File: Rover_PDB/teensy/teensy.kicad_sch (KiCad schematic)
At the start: 14 parts, among them J1 Conn_01x04, J2 Conn_01x04, J3 Conn_01x04, M1 Fan, M2 Fan, M3 Fan, Q1 Q_NMOS, Q2 Q_NMOS, U1 Teensy4.1, U2 MCP9808_MSOP

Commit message: update
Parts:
- removed Q1, Q2: Q_NMOS, Package_TO_SOT_THT:TO-92_Inline, symbol Device:Q_NMOS
- added C2, C4: 100nF, Capacitor_SMD:C_01005_0402Metric, symbol Device:C_Small
- added C3: 50nF, Capacitor_SMD:C_01005_0402Metric, symbol Device:C_Small
- added Q1, Q2: NMOS, Package_TO_SOT_THT:TO-220-3_Vertical, symbol Simulation_SPICE:NMOS
- C1: footprint Package_TO_SOT_SMD:SOT-23-6 -> Capacitor_SMD:C_01005_0402Metric
- R1, R2, R3: footprint Package_DIP:DIP-8_W7.62mm -> Resistor_SMD:R_01005_0402Metric
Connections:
- net GND: now also C1.1, C1.2, J3.2 (Pin_2), U1.45 (23_A9_CRX1_MCLK1), U1.47 (GND), U1.58 (GND), U2.8 (V_{DD}), C2.2, C3.2, Q1.3 (S), Q2.3 (S)
- net SCL_BMS_TEAM: no longer U1.41 (19_A5_SCL), U2.2 (SCL)
- net SDA_BMS_TEAM: no longer U1.40 (18_A4_SDA), U2.1 (SDA)
- net at M1.2 (-), M2.2 (-), M3.2 (-): now also Q2.1 (D)
- net at R2.2: now also C3.1, Q1.1 (D), Q2.2 (G)
- net at R1.1, U1.44 (22_A8_CTX1): now also C2.1
- net at U1.48 (VIN): now also C4.1, C4.2
- net +3V3: now reaches U1.51 (3V3)
- net +3V3: now also J3.1 (Pin_1)
- net at R1.2: now also Q1.2 (G)
- new net SCL: U2.2 (SCL)
- new net SDA: U2.1 (SDA)
- no-connect marks 62 -> 57

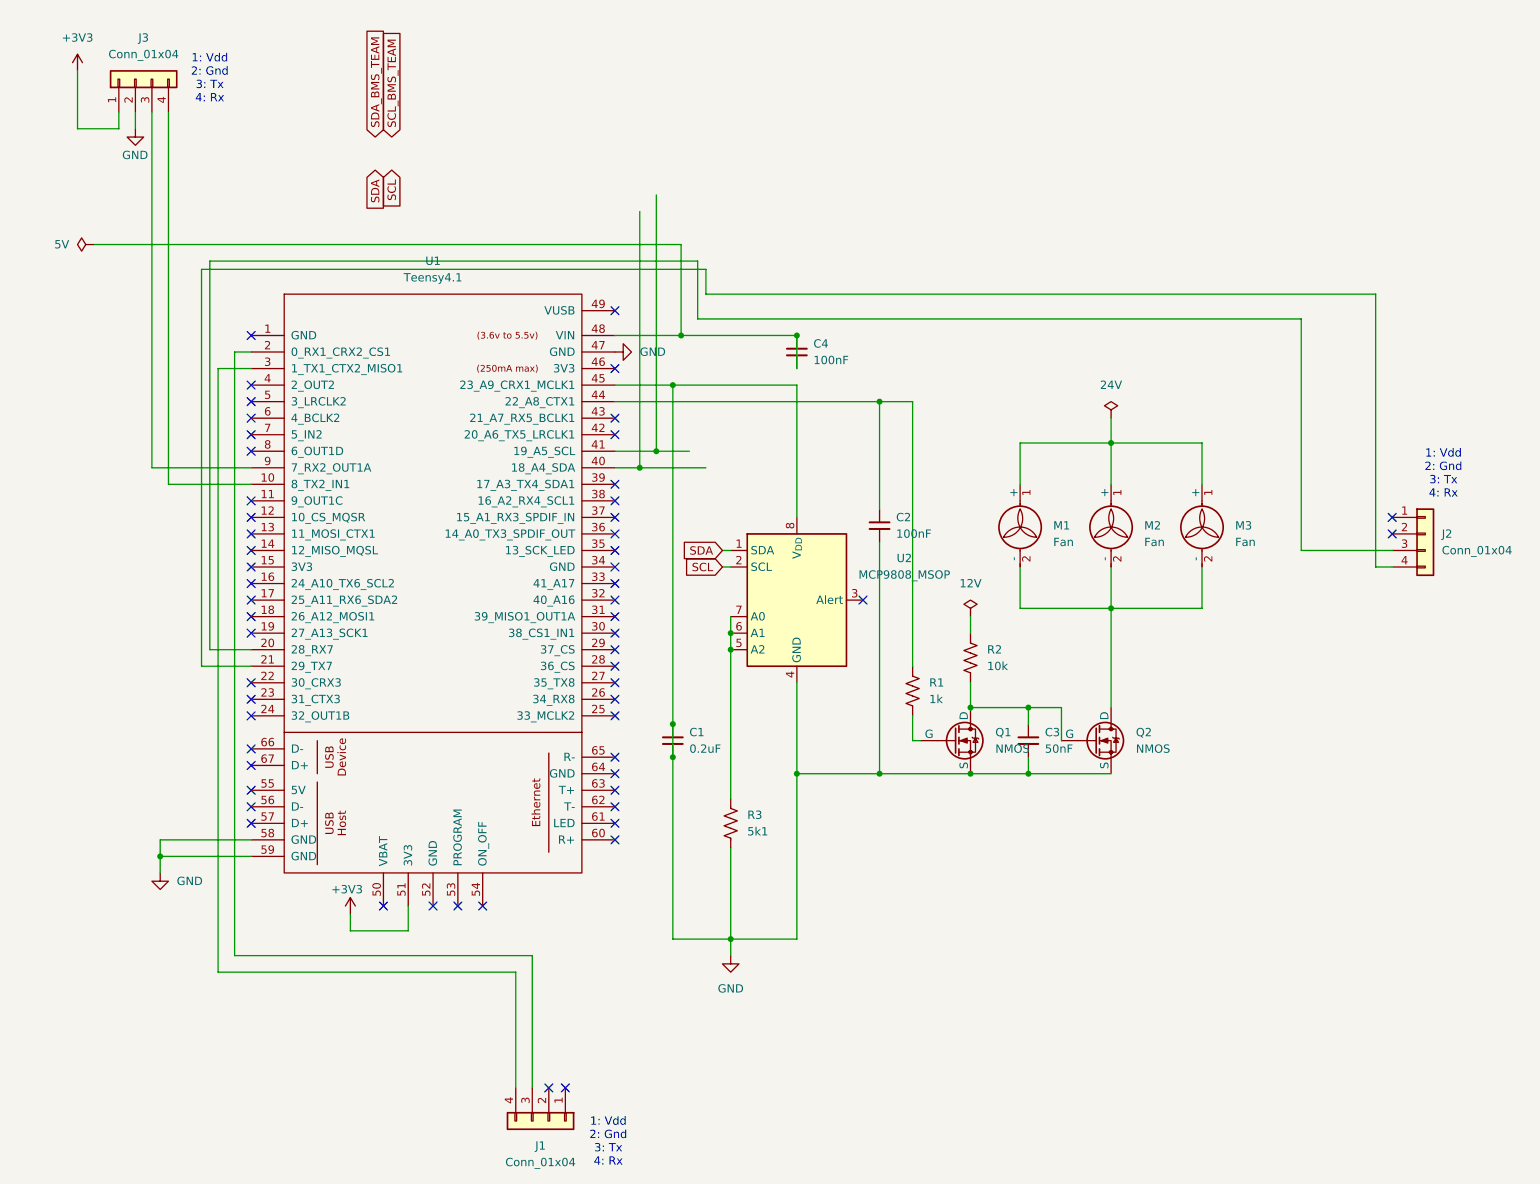
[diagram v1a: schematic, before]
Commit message: Changed connector positions so there are fewer crossovers; connected BMS to its own I2C bus
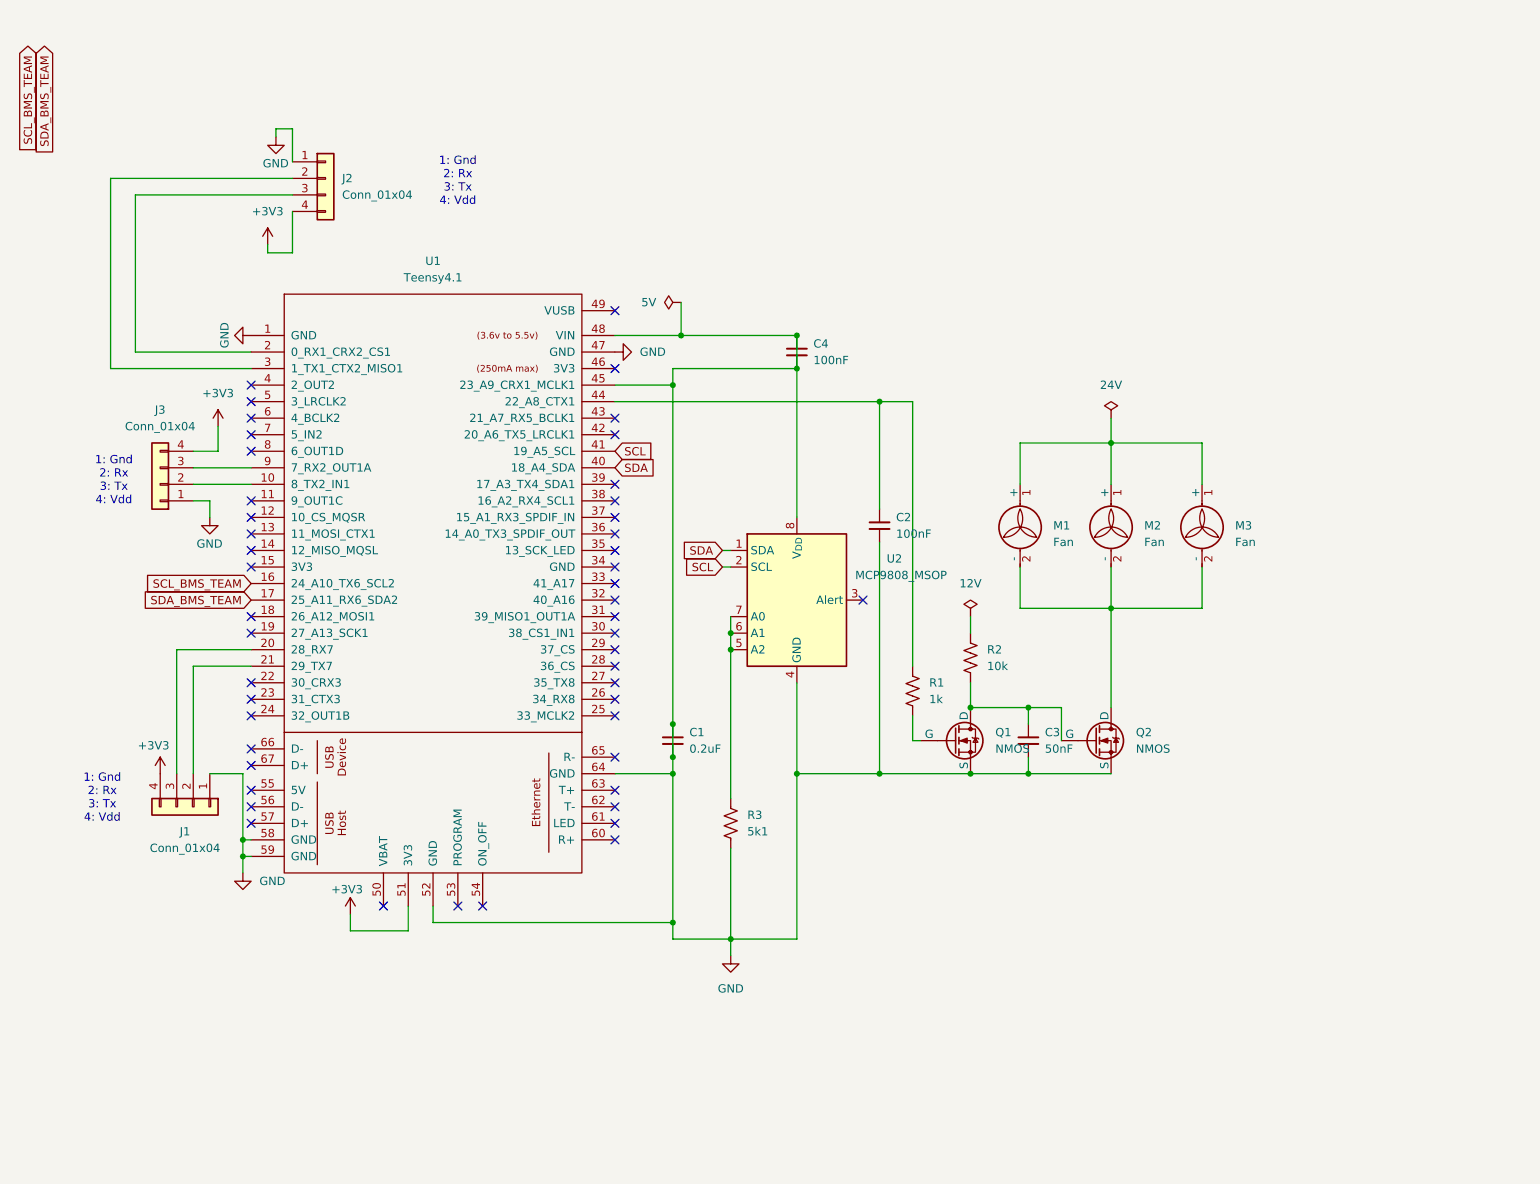
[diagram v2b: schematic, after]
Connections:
- net +3V3: now also J1.4 (Pin_4), J2.4 (Pin_4), J3.4 (Pin_4); no longer J3.1 (Pin_1)
- net GND: now also C4.1, C4.2, J1.1 (Pin_1), J2.1 (Pin_1), J3.1 (Pin_1), U1.1 (GND), U1.48 (VIN), U1.52 (GND), U1.64 (GND); no longer J3.2 (Pin_2)
- net SCL: now also U1.41 (19_A5_SCL)
- net SCL_BMS_TEAM: now also U1.16 (24_A10_TX6_SCL2)
- net SDA: now also U1.40 (18_A4_SDA)
- net SDA_BMS_TEAM: now also U1.17 (25_A11_RX6_SDA2)
- net at U1.10 (8_TX2_IN1): now also J3.2 (Pin_2); no longer J3.4 (Pin_4)
- net at U1.2 (0_RX1_CRX2_CS1): now also J2.3 (Pin_3); no longer J1.3 (Pin_3)
- net at U1.20 (28_RX7): now also J1.3 (Pin_3); no longer J2.3 (Pin_3)
- net at U1.21 (29_TX7): now also J1.2 (Pin_2); no longer J2.4 (Pin_4)
- net at U1.3 (1_TX1_CTX2_MISO1): now also J2.2 (Pin_2); no longer J1.4 (Pin_4)
- no-connect marks 57 -> 48
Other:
- note added: "1: Gnd 2: Rx 3: Tx 4: Vdd"
- note removed: "1: Vdd 2: Gnd 3: Tx 4: Rx"
- moved on the sheet: J1, J2, J3
